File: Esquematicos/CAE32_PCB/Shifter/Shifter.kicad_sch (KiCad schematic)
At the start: 26 parts, among them J1 EXP-PORT, J2 SPI_DEVICE, J3 Conn_01x08_Female, J4 Conn_01x08_Female, J5 Conn_01x08_Female, SW1 USB_BOOT, U1 RP2040, U2 W25Q128JVS, Y1 12Mhz

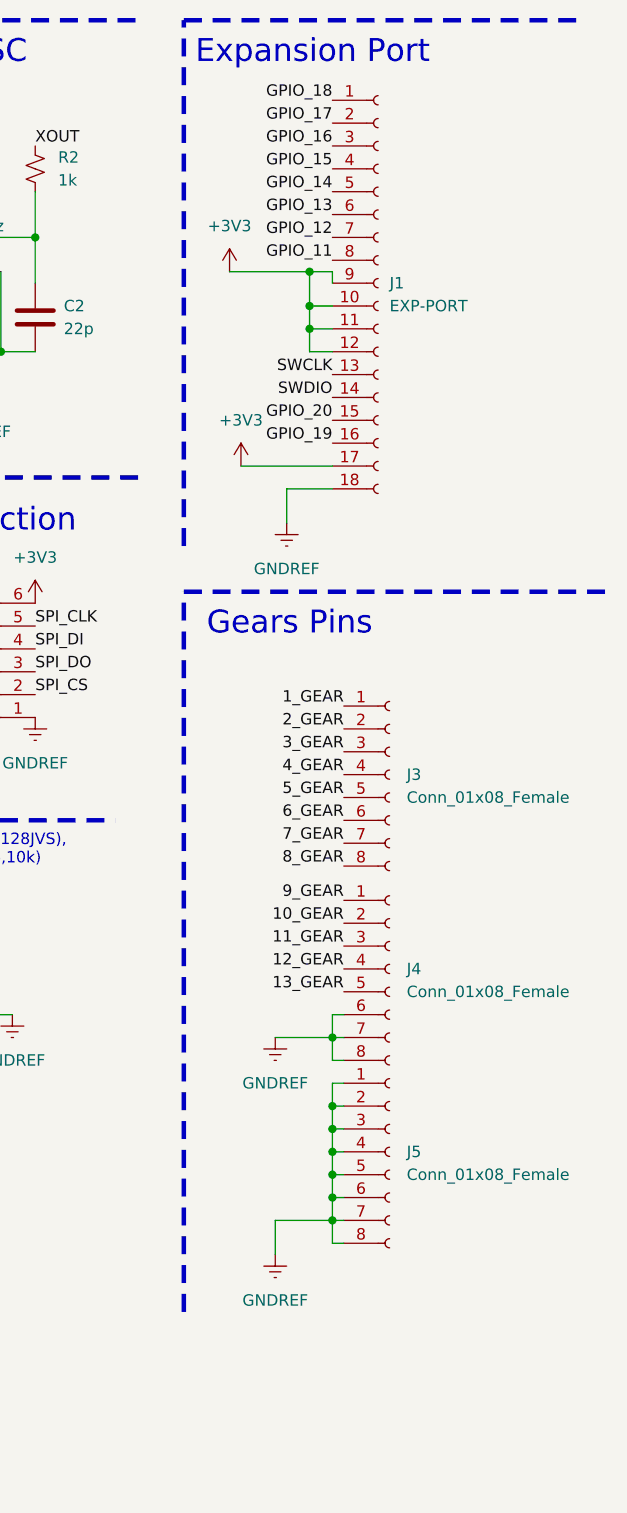
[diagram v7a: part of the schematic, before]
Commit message: update: redesign of the shifter PCB, changing the PCB requirements(via from 0.15 to 0.3mm) and pin sockets for FCP connectors
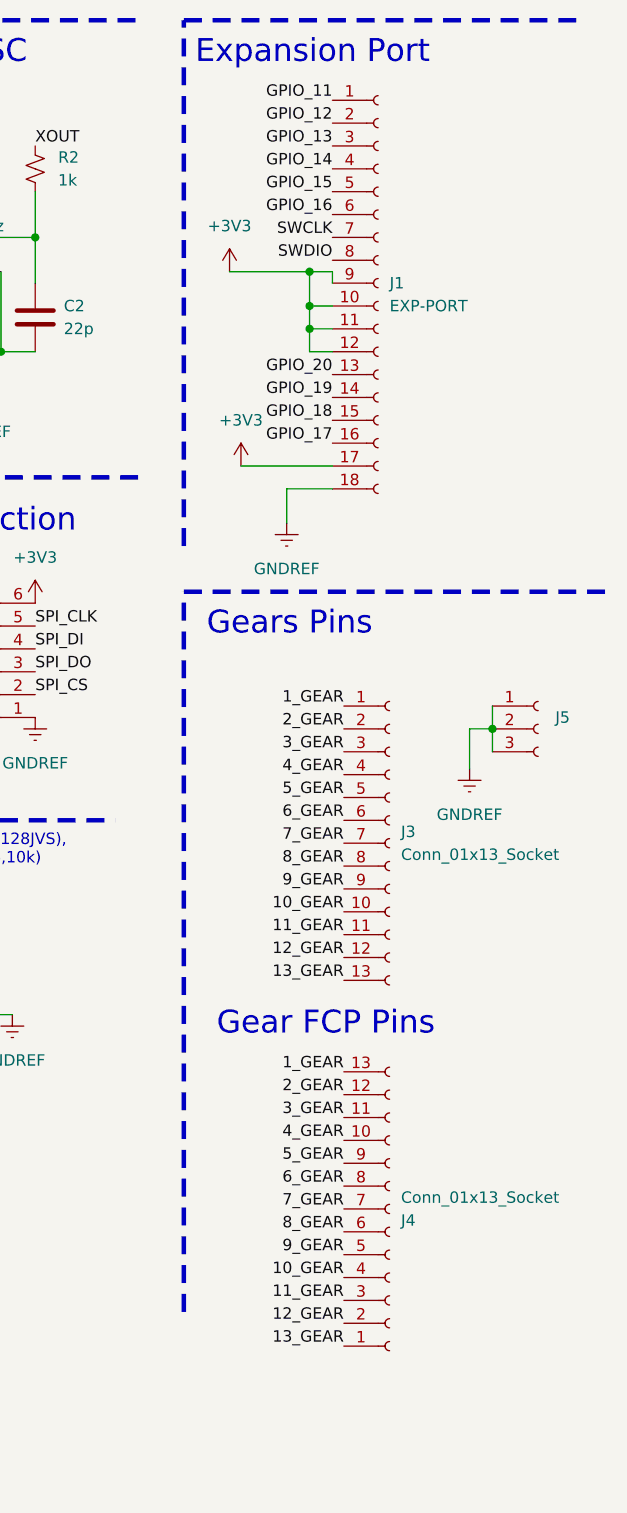
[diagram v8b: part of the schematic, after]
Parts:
- removed J3, J4, J5: Conn_01x08_Female, Connector_PinSocket_2.54mm:PinSocket_1x08_P2.54mm_Vertical, symbol Connector:Conn_01x08_Female
- added J3: Conn_01x13_Socket, shifter:Pad_1x13_THT_1.27mm, symbol Connector:Conn_01x13_Socket
- added J4: Conn_01x13_Socket, Connector_FFC-FPC:Hirose_FH12-13S-0.5SH_1x13-1MP_P0.50mm_Horizontal, symbol Connector:Conn_01x13_Socket
- added J5: Conn_01x03_Socket, Connector_PinHeader_2.54mm:PinHeader_1x03_P2.54mm_Vertical, symbol Connector:Conn_01x03_Socket
- J1: footprint shifter:BM28B0-6-16DS -> Connector_FFC-FPC:Hirose_FH12-18S-0.5SH_1x18-1MP_P0.50mm_Horizontal
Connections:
- net 10_GEAR: now also J3.10 (Pin_10), J4.4 (Pin_4)
- net 11_GEAR: now also J3.11 (Pin_11), J4.3 (Pin_3)
- net 12_GEAR: now also J3.12 (Pin_12), J4.2 (Pin_2)
- net 13_GEAR: now also J3.13 (Pin_13), J4.1 (Pin_1)
- net 1_GEAR: now also J3.1 (Pin_1), J4.13 (Pin_13)
- net 2_GEAR: now also J3.2 (Pin_2), J4.12 (Pin_12)
- net 3_GEAR: now also J3.3 (Pin_3), J4.11 (Pin_11)
- net 4_GEAR: now also J3.4 (Pin_4), J4.10 (Pin_10)
- net 5_GEAR: now also J3.5 (Pin_5), J4.9 (Pin_9)
- net 6_GEAR: now also J3.6 (Pin_6), J4.8 (Pin_8)
- net 7_GEAR: now also J3.7 (Pin_7), J4.7 (Pin_7)
- net 8_GEAR: now also J3.8 (Pin_8), J4.6 (Pin_6)
- net 9_GEAR: now also J3.9 (Pin_9), J4.5 (Pin_5)
- net GNDREF: now also J5.1 (Pin_1), J5.2 (Pin_2), J5.3 (Pin_3)
- net GPIO_11: now also J1.1 (Pin_1); no longer J1.8 (Pin_8)
- net GPIO_12: now also J1.2 (Pin_2); no longer J1.7 (Pin_7)
- net GPIO_13: now also J1.3 (Pin_3); no longer J1.6 (Pin_6)
- net GPIO_14: now also J1.4 (Pin_4); no longer J1.5 (Pin_5)
- net GPIO_15: now also J1.5 (Pin_5); no longer J1.4 (Pin_4)
- net GPIO_16: now also J1.6 (Pin_6); no longer J1.3 (Pin_3)
- net GPIO_17: now also J1.16 (Pin_16); no longer J1.2 (Pin_2)
- net GPIO_18: now also J1.15 (Pin_15); no longer J1.1 (Pin_1)
- net GPIO_19: now also J1.14 (Pin_14); no longer J1.16 (Pin_16)
- net GPIO_20: now also J1.13 (Pin_13); no longer J1.15 (Pin_15)
- net SWCLK: now also J1.7 (Pin_7); no longer J1.13 (Pin_13)
- net SWDIO: now also J1.8 (Pin_8); no longer J1.14 (Pin_14)
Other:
- note added: "Gear FCP Pins"
